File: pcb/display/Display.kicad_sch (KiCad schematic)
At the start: 32 parts, among them J101 RJ45, J102 Screw Terminal 3.5mm, J103 01x08_Pin, P101 USB_C_Plug_USB2.0, Q101 2N7002, SW101 SW_4x3mm, SW102 SW_4x3mm, SW103 SW_4x3mm, SW104 SW_4x3mm, U101 TMP1075DSGR, U102 ESP32-S3-MINI-1U-N8

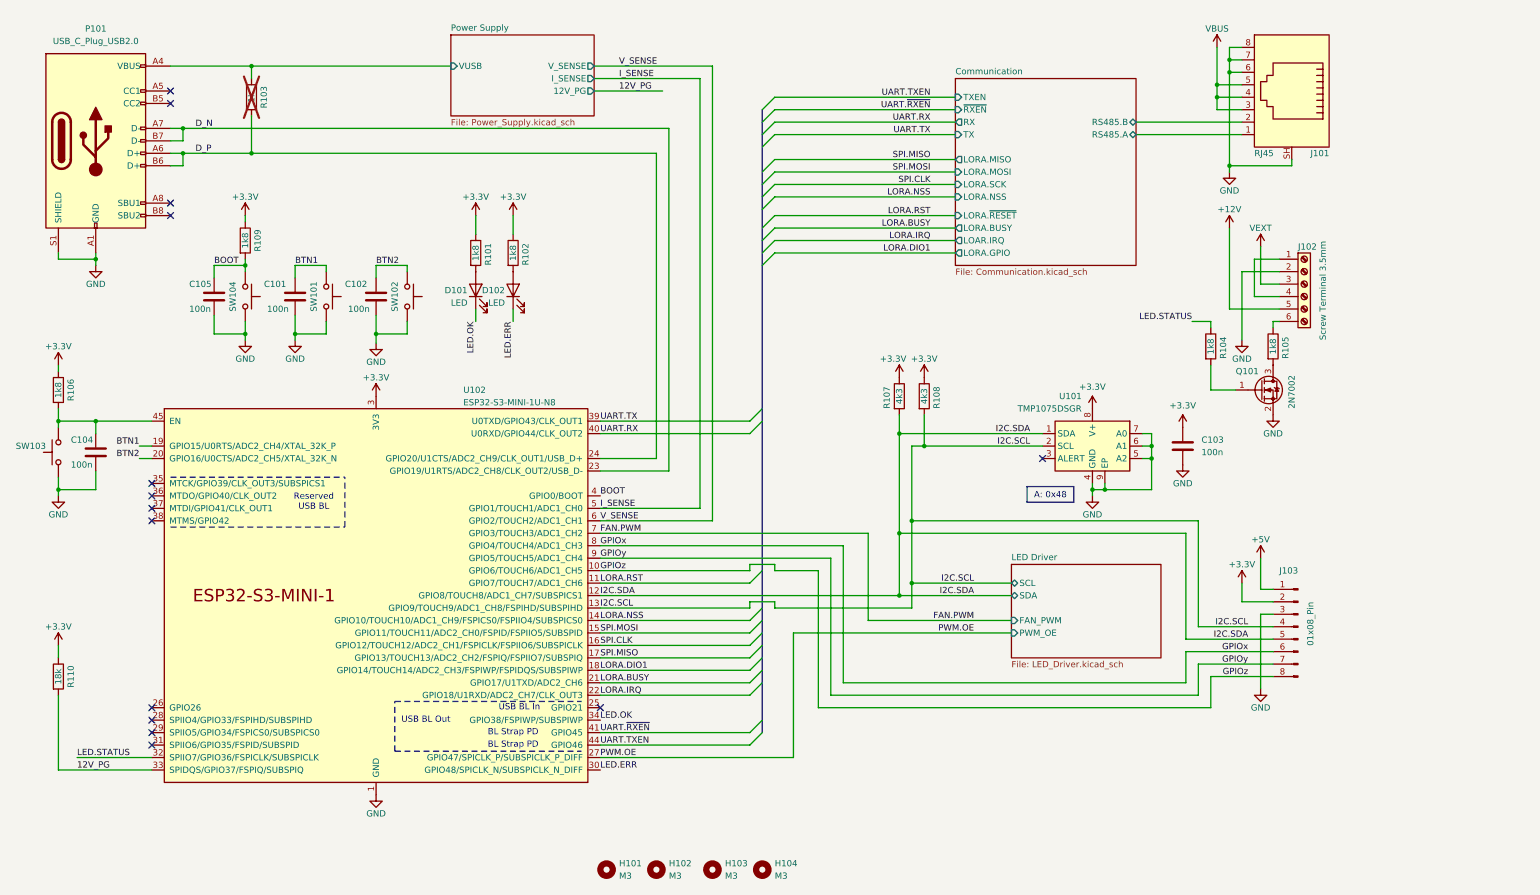
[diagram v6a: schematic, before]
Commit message: OSC Display Hardware Revision 02
There might still be some errors which need to be corrected during ordering.
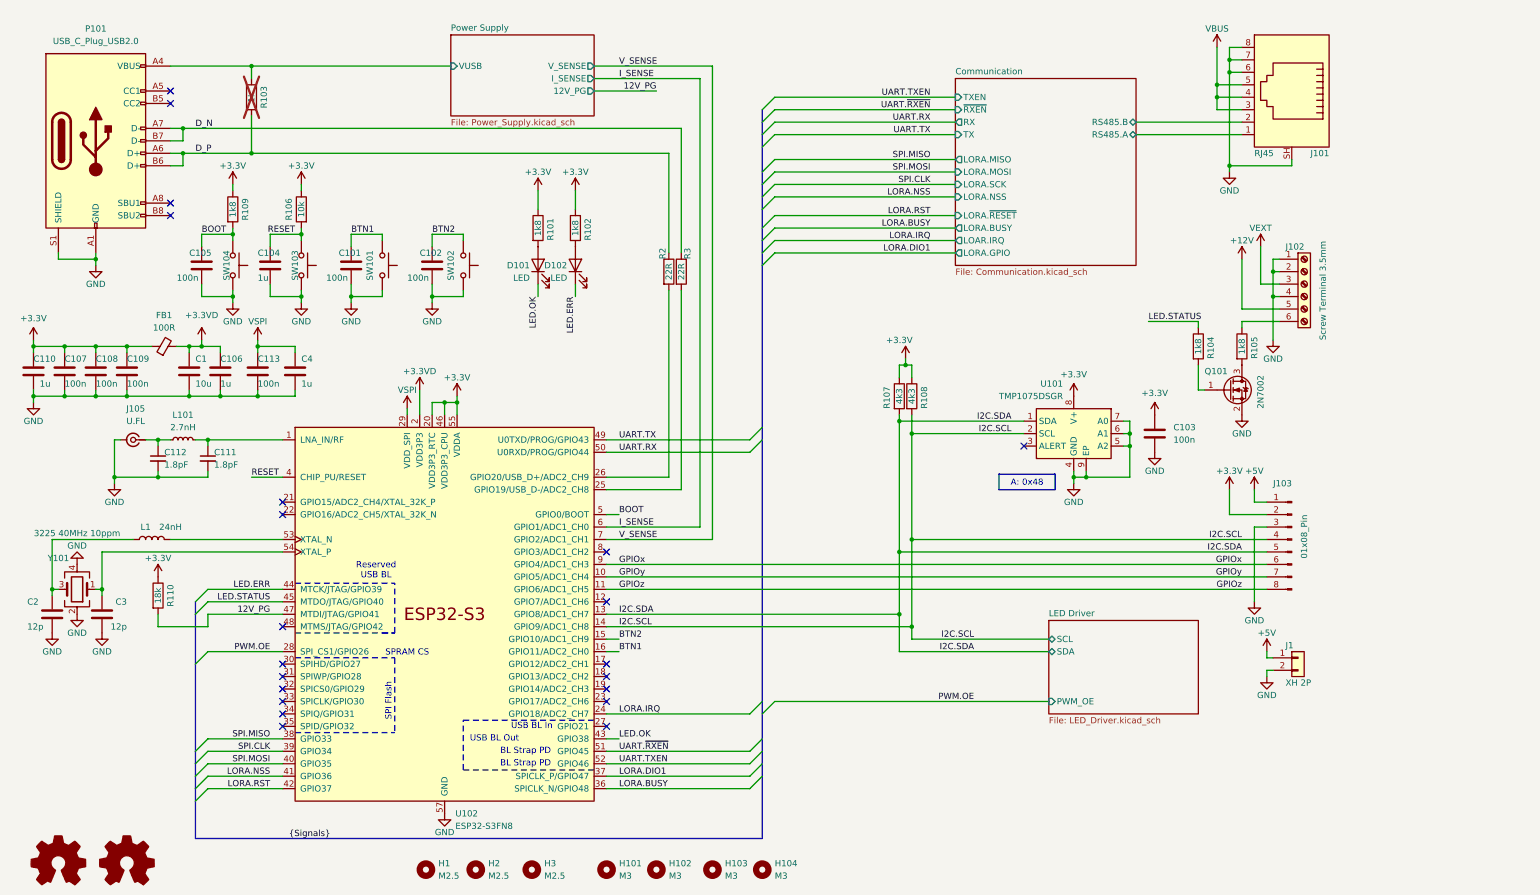
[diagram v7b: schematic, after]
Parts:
- removed U102: ESP32-S3-MINI-1U-N8, Espressif:ESP32-S3-MINI-1U, symbol Espressif:ESP32-S3-MINI-1
- added C1: 10u, Capacitor_SMD:C_0603_1608Metric, symbol Device:C
- added C106, C110, C4: 1u, Capacitor_SMD:C_0402_1005Metric, symbol Device:C
- added C107, C108, C109, C113: 100n, Capacitor_SMD:C_0402_1005Metric, symbol Device:C
- added C111, C112: 1.8pF, Capacitor_SMD:C_0402_1005Metric, symbol Device:C_Small
- added C2, C3: 12p, Capacitor_SMD:C_0402_1005Metric, symbol Device:C
- added FB1: 100R, Inductor_SMD:L_0603_1608Metric, symbol Device:FerriteBead_Small
- added H1, H2, H3: M2.5, MountingHole:MountingHole_2.7mm_M2.5_DIN965, symbol Mechanical:MountingHole
- added J1: XH 2P, Connector_JST:JST_XH_B2B-XH-A_1x02_P2.50mm_Vertical, symbol Connector_Generic:Conn_01x02
- added J105: U.FL, RVNSPRK_Connector:U.FL_Hirose_U.FL-R-SMT-1_Vertical, symbol Connector:Conn_Coaxial_Small
- added L1: 24nH, Inductor_SMD:L_0402_1005Metric, symbol Device:L
- added L101: 2.7nH, Inductor_SMD:L_0402_1005Metric, symbol Device:L_Small
- added R2, R3: 22R, Resistor_SMD:R_0402_1005Metric, symbol Device:R
- added SYM1: Logo_Open_Hardware_Small, Symbol:OSHW-Logo2_7.3x6mm_SilkScreen, symbol Graphic:Logo_Open_Hardware_Small
- added SYM2: Logo_Open_Hardware_Small, Symbol:KiCad-Logo2_5mm_SilkScreen, symbol Graphic:Logo_Open_Hardware_Small
- added U102: ESP32-S3FN8, Package_DFN_QFN:QFN-56-1EP_7x7mm_P0.4mm_EP5.6x5.6mm, symbol Espressif:ESP32-S3
- added Y101: 3225 40MHz 10ppm, Crystal:Crystal_SMD_3225-4Pin_3.2x2.5mm, symbol Device:Crystal_GND24
- C101, C102, C103, C105: JLC PN C307331 -> (none); LCSC Part # (none) -> C307331
- C104: value 100n -> 1u; JLC PN C307331 -> (none); LCSC Part # (none) -> C52923
- D101, D102: JLC PN C2286 -> (none); LCSC Part # (none) -> C2286
- J101: JLC PN C19078599 -> (none); LCSC Part # (none) -> C19078599
- J102: JLC PN C409119 -> (none); LCSC Part # (none) -> C409119
- P101: JLC PN C2927039 -> (none); LCSC Part # (none) -> C2927039
- Q101: JLC PN C8545 -> (none); LCSC Part # (none) -> C8545
- R106: value 1k8 -> 10k
- SW101, SW102, SW103, SW104: JLC PN C18077679 -> (none); LCSC Part # (none) -> C18077679
- U101: JLC PN C2870250 -> (none); LCSC Part # (none) -> C2870250
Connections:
- net +3.3V: now also C107.1, C108.1, C109.1, C110.1, FB1.1, U102.20 (VDD3P3_RTC), U102.46 (VDD3P3_CPU), U102.55 (VDDA), U102.56 (VDDA)
- net +5V: now also J1.1 (Pin_1)
- net 12V_PG: now also U102.47 (MTDI/JTAG/GPIO41)
- net BOOT: now also U102.5 (GPIO0/BOOT)
- net BTN1: now also U102.16 (GPIO11/ADC2_CH0)
- net BTN2: now also U102.15 (GPIO10/ADC1_CH9)
- net D_N: now also R3.1
- net D_P: now also R2.1
- net GND: now also J102.1 (Pin_1), J102.4 (Pin_4), C1.2, C106.2, C107.2, C108.2, C109.2, C110.2, C111.2, C112.2, C113.2, C2.2, C3.2, C4.2, J1.2 (Pin_2), J105.2 (Ext), U102.57 (GND), Y101.2, Y101.4
- net GPIOx: now also U102.9 (GPIO4/ADC1_CH3)
- net GPIOy: now also U102.10 (GPIO5/ADC1_CH4)
- net GPIOz: now also U102.11 (GPIO6/ADC1_CH5)
- net I2C.SCL: now also U102.14 (GPIO9/ADC1_CH8)
- net I2C.SDA: now also U102.13 (GPIO8/ADC1_CH7)
- net I_SENSE: now also U102.6 (GPIO1/ADC1_CH0)
- net LED.ERR: now also U102.44 (MTCK/JTAG/GPIO39)
- net LED.OK: now also U102.43 (GPIO38)
- net LED.STATUS: now also U102.45 (MTDO/JTAG/GPIO40)
- net LORA.BUSY: now also U102.36 (SPICLK_N/GPIO48)
- net LORA.DIO1: now also U102.37 (SPICLK_P/GPIO47)
- net LORA.IRQ: now also U102.24 (GPIO18/ADC2_CH7)
- net LORA.NSS: now also U102.41 (GPIO36)
- net LORA.RST: now also U102.42 (GPIO37)
- net PWM.OE: now also U102.28 (SPI_CS1/GPIO26)
- net SPI.CLK: now also U102.39 (GPIO34)
- net SPI.MISO: now also U102.38 (GPIO33)
- net SPI.MOSI: now also U102.40 (GPIO35)
- net UART.RX: now also U102.50 (U0RXD/PROG/GPIO44)
- net UART.TX: now also U102.49 (U0TXD/PROG/GPIO43)
- net UART.TXEN: now also U102.52 (GPIO46)
- net UART.~{RXEN}: now also U102.51 (GPIO45)
- net V_SENSE: now also U102.7 (GPIO2/ADC1_CH1)
- net RESET: now reaches C104.1, R106.2, SW103.1
- net RESET: now also U102.4 (CHIP_PU/RESET)
- new net: C111.1, L101.2, U102.1 (LNA_IN/RF)
- new net: R3.2, U102.25 (GPIO19/USB_D-/ADC2_CH8)
- new net: R2.2, U102.26 (GPIO20/USB_D+/ADC2_CH9)
- new net: L1.2, U102.53 (XTAL_N)
- new net: C3.1, U102.54 (XTAL_P), Y101.1
- new net: C2.1, L1.1, Y101.3
- new net: C112.1, J105.1 (In), L101.1
- new net +3.3VD: C1.1, C106.1, FB1.2, U102.2 (VDD3P3), U102.3 (VDD3P3)
- new net VSPI: C113.1, C4.1, U102.29 (VDD_SPI)
- no-connect marks 14 -> 21
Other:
- sheet LED Driver ports: added none; removed FAN_PWM
- note added: "SPI Flash"
- note added: "SPRAM CS"
- moved on the sheet: C101, C102, C103, C104, C105, D101, D102, J103, Q101, R101, R102, R104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
